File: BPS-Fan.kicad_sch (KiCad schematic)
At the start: 29 parts, among them J1 LDRBRDConn, J10 FAN9, J11 FAN10, J12 FAN11, J13 FAN12, J2 FAN1, J3 FAN2, J4 FAN3, J5 FAN4, J6 FAN5, J7 FAN6, J8 FAN7, J9 FAN8, Q1 BUK9M23-80E, Q10 BUK9M23-80E, Q4 BUK9M23-80E, Q7 BUK9M23-80E

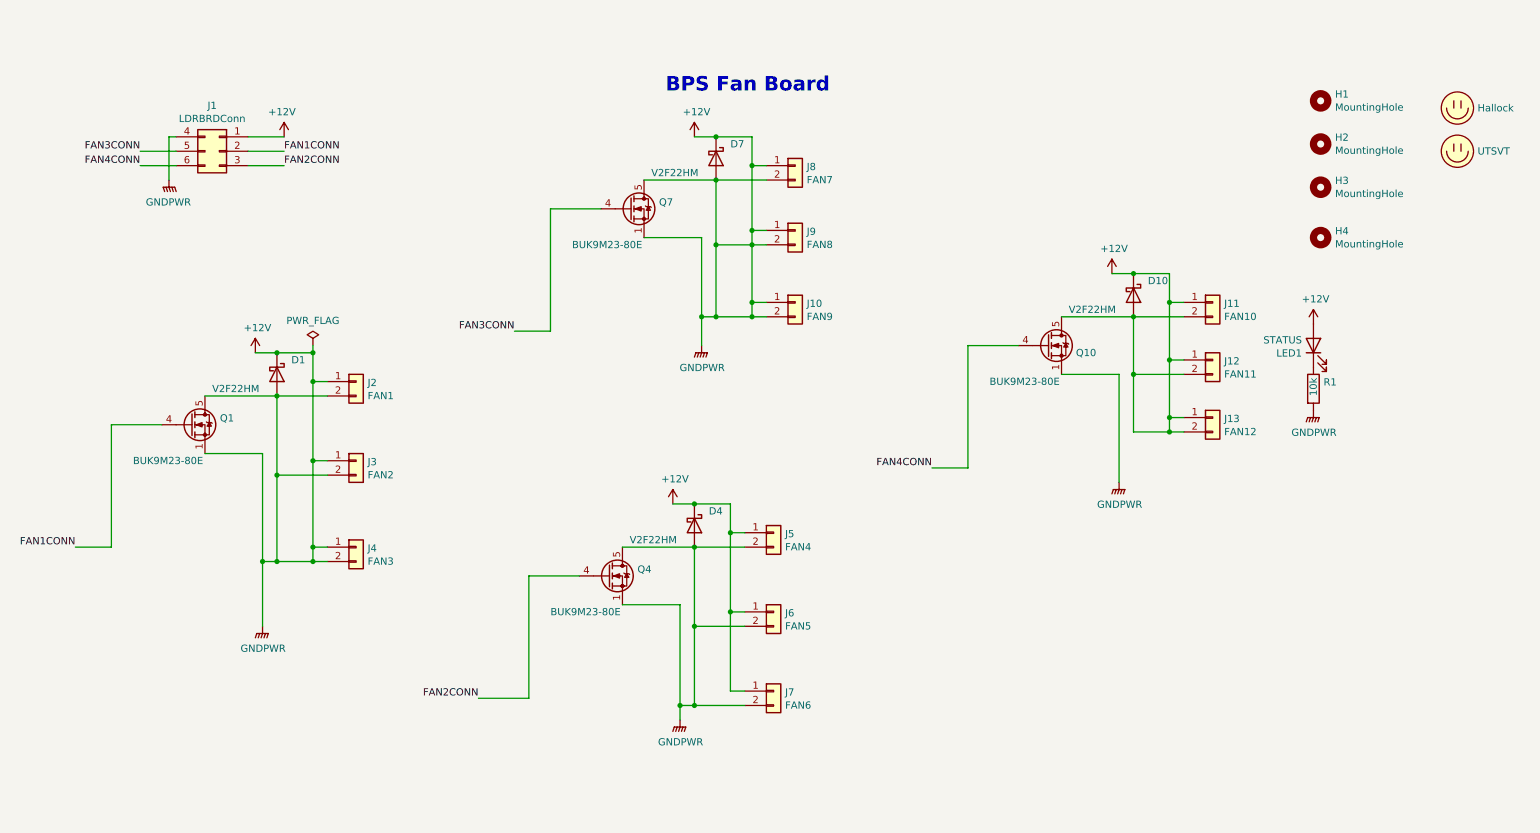
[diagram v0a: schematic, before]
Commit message: cleaned up schematic and fixed shorts
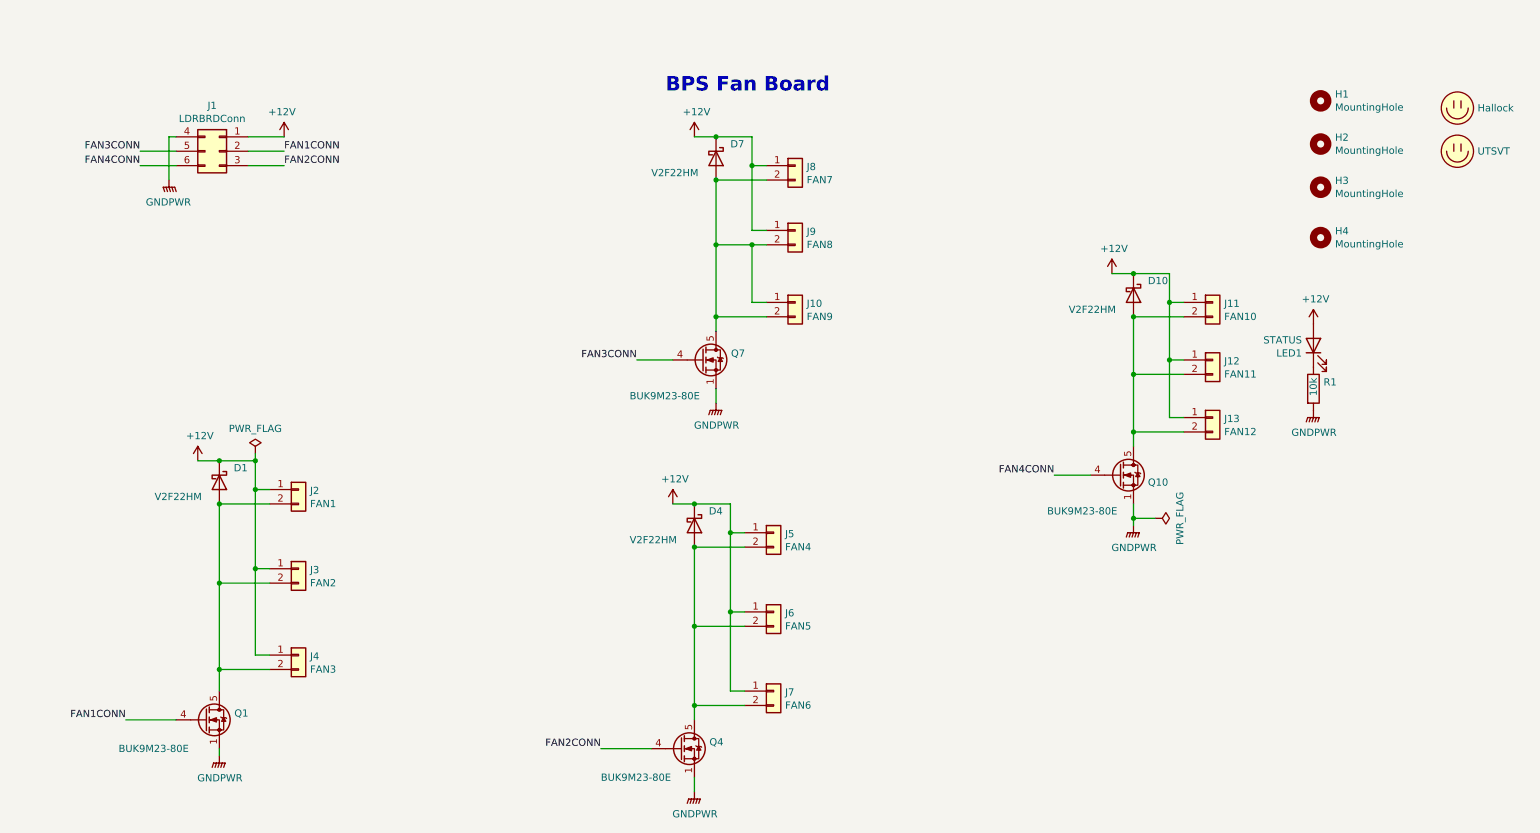
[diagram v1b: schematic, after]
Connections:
- net +12V: no longer D1.2 (A), D10.2 (A), D4.2 (A), D7.2 (A), J1.4 (Pin_4), J10.1 (Pin_1), J10.2 (Pin_2), J11.2 (Pin_2), J12.2 (Pin_2), J13.2 (Pin_2), J2.2 (Pin_2), J3.2 (Pin_2), J4.2 (Pin_2), J5.2 (Pin_2), J6.2 (Pin_2), J7.2 (Pin_2), J8.2 (Pin_2), J9.2 (Pin_2), Q1.1 (S), Q1.2 (S), Q1.3 (S), Q1.5 (D), Q10.1 (S), Q10.2 (S), Q10.3 (S), Q10.5 (D), Q4.1 (S), Q4.2 (S), Q4.3 (S), Q4.5 (D), Q7.1 (S), Q7.2 (S), Q7.3 (S), Q7.5 (D), R1.2
- new net: D10.2 (A), J11.2 (Pin_2), J12.2 (Pin_2), J13.2 (Pin_2), Q10.5 (D)
- new net: D1.2 (A), J2.2 (Pin_2), J3.2 (Pin_2), J4.2 (Pin_2), Q1.5 (D)
- new net: D4.2 (A), J5.2 (Pin_2), J6.2 (Pin_2), J7.2 (Pin_2), Q4.5 (D)
- new net: D7.2 (A), J10.1 (Pin_1), J10.2 (Pin_2), J8.2 (Pin_2), J9.2 (Pin_2), Q7.5 (D)
- new net GNDPWR: J1.4 (Pin_4), Q1.1 (S), Q1.2 (S), Q1.3 (S), Q10.1 (S), Q10.2 (S), Q10.3 (S), Q4.1 (S), Q4.2 (S), Q4.3 (S), Q7.1 (S), Q7.2 (S), Q7.3 (S), R1.2
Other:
- moved on the sheet: D1, J2, J3, J4, Q1, Q10, Q4, Q7

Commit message: fixed the last short lol
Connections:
- net +12V: now also J10.1 (Pin_1)
- net at D7.2 (A), J10.2 (Pin_2), J8.2 (Pin_2)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: no longer J10.1 (Pin_1)

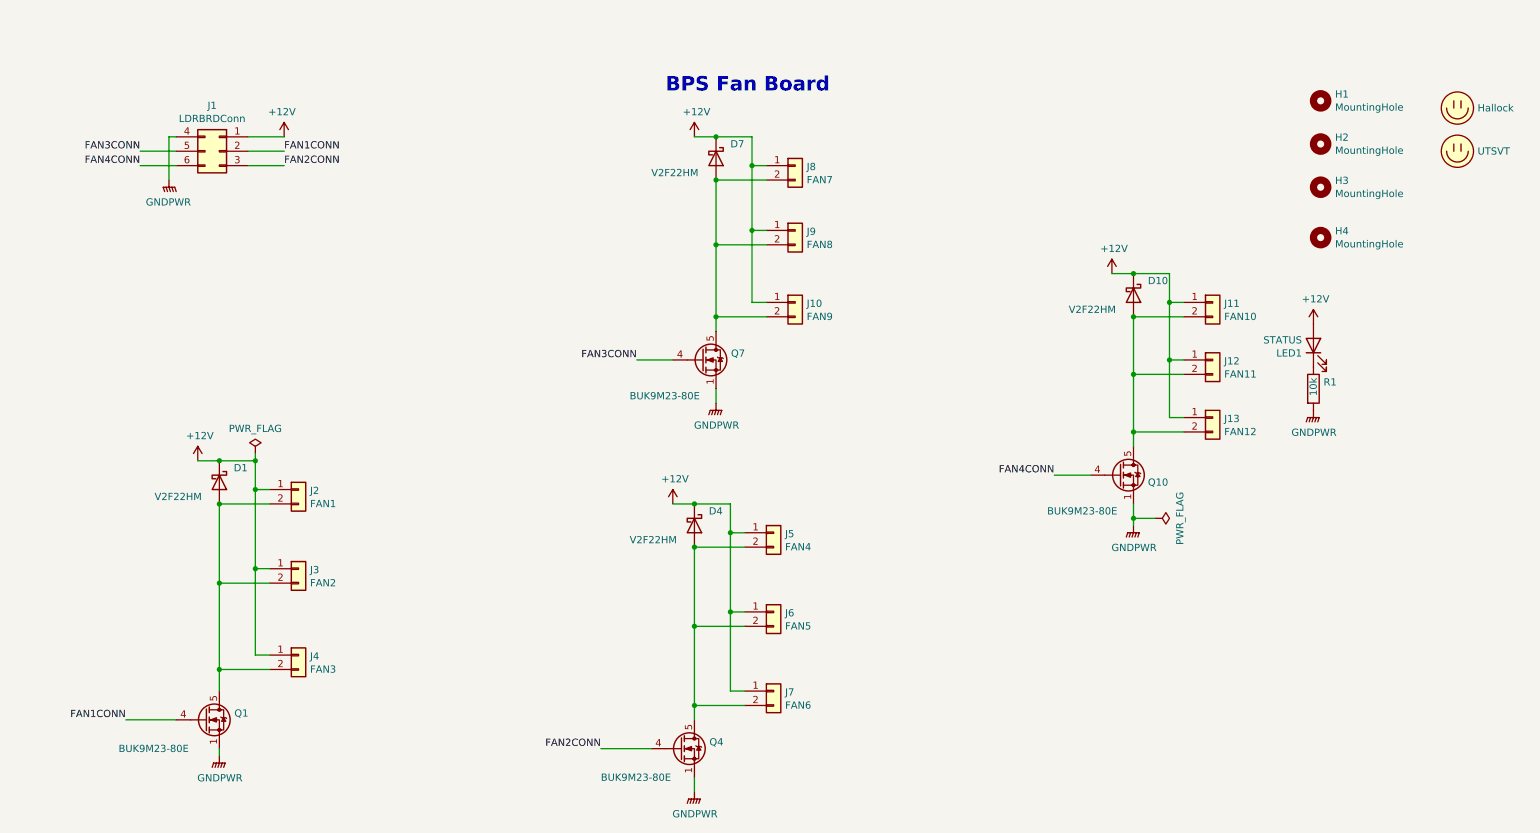
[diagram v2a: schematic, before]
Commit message: Added support for Orion
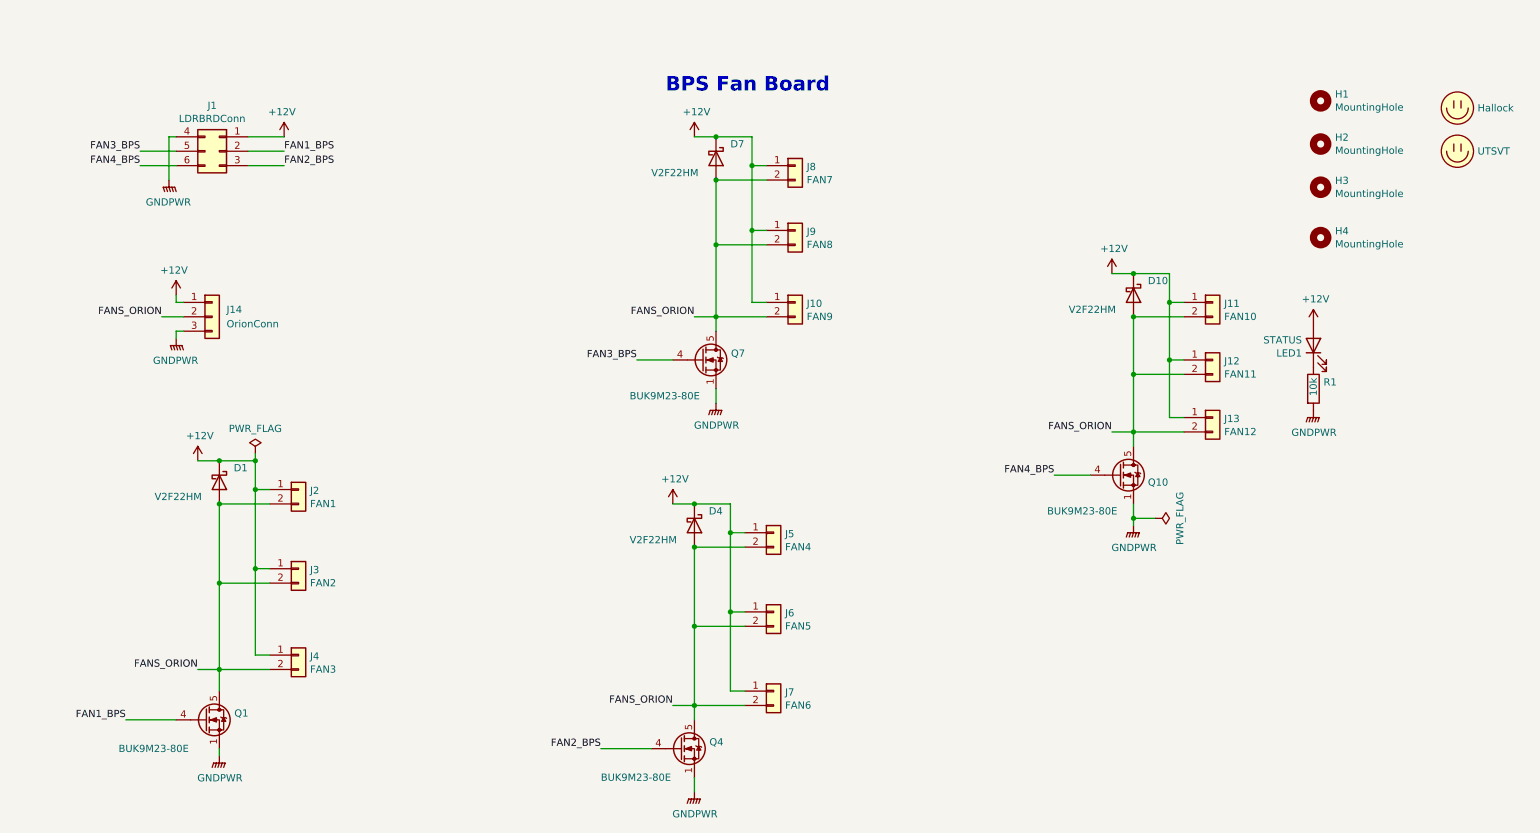
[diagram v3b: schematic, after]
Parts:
- added J14: OrionConn, symbol Connector_Generic:Conn_01x03
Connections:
- net +12V: now also J14.1 (Pin_1)
- net GNDPWR: now also J14.3 (Pin_3)
- net FANS_ORION: now reaches D10.2 (A), J11.2 (Pin_2), J12.2 (Pin_2), J13.2 (Pin_2), Q10.5 (D)
- net FANS_ORION: now also D1.2 (A), D4.2 (A), D7.2 (A), J10.2 (Pin_2), J2.2 (Pin_2), J3.2 (Pin_2), J4.2 (Pin_2), J5.2 (Pin_2), J6.2 (Pin_2), J7.2 (Pin_2), J8.2 (Pin_2), J9.2 (Pin_2), Q1.5 (D), Q4.5 (D), Q7.5 (D), J14.2 (Pin_2)
- net FAN1CONN renamed FAN1_BPS
- net FAN2CONN renamed FAN2_BPS
- net FAN3CONN renamed FAN3_BPS
- net FAN4CONN renamed FAN4_BPS
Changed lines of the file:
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@@
+    (stroke (width 0) (type default) (color 0 0 0 0))
+  )
+  (wire (pts (xy 208.28 115.57) (xy 212.09 115.57))
     (stroke (width 0) (type default) (color 0 0 0 0))
   )
@@
     (stroke (width 0) (type default) (color 0 0 0 0))
   )
+  (wire (pts (xy 134.62 95.25) (xy 138.43 95.25))
+    (stroke (width 0) (type default) (color 0 0 0 0))
+  )
   (wire (pts (xy 212.09 115.57) (xy 212.09 118.11))
     (stroke (width 0) (type default) (color 0 0 0 0))
@@
     (stroke (width 0) (type default) (color 0 0 0 0))
   )
+  (wire (pts (xy 44.45 97.79) (xy 43.18 97.79))
+    (stroke (width 0) (type default) (color 0 0 0 0))
+  )
   (wire (pts (xy 134.62 135.89) (xy 134.62 149.86))
     (stroke (width 0) (type default) (color 0 0 0 0))
@@
     (stroke (width 0) (type default) (color 0 0 0 0))
   )
+  (wire (pts (xy 43.18 92.71) (xy 44.45 92.71))
+    (stroke (width 0) (type default) (color 0 0 0 0))
+  )
   (wire (pts (xy 43.18 63.5) (xy 41.91 63.5))
     (stroke (width 0) (type default) (color 0 0 0 0))
@@
     (stroke (width 0) (type default) (color 0 0 0 0))
   )
+  (wire (pts (xy 43.18 97.79) (xy 43.18 99.06))
+    (stroke (width 0) (type default) (color 0 0 0 0))
+  )
   (wire (pts (xy 50.8 128.27) (xy 50.8 142.24))
     (stroke (width 0) (type default) (color 0 0 0 0))
@@
     (stroke (width 0) (type default) (color 0 0 0 0))
   )
+  (wire (pts (xy 138.43 82.55) (xy 147.32 82.55))
+    (stroke (width 0) (type default) (color 0 0 0 0))
+  )
+  (wire (pts (xy 134.62 176.53) (xy 134.62 179.07))
+    (stroke (width 0) (type default) (color 0 0 0 0))
+  )
+  (wire (pts (xy 43.18 91.44) (xy 43.18 92.71))
+    (stroke (width 0) (type default) (color 0 0 0 0))
+  )
+  (wire (pts (xy 140.97 128.27) (xy 134.62 128.27))
+    (stroke (width 0) (type default) (color 0 0 0 0))
+  )
+  (wire (pts (xy 62.23 63.5) (xy 55.88 63.5))
+    (stroke (width 0) (type default) (color 0 0 0 0))
+  )
+  (wire (pts (xy 140.97 133.35) (xy 140.97 147.32))
+    (stroke (width 0) (type default) (color 0 0 0 0))
+  )
+  (wire (pts (xy 130.81 163.83) (xy 134.62 163.83))
+    (stroke (width 0) (type default) (color 0 0 0 0))
+  )
+  (wire (pts (xy 59.69 154.94) (xy 57.15 154.94))
+    (stroke (width 0) (type default) (color 0 0 0 0))
+  )
+  (wire (pts (xy 218.44 87.63) (xy 212.09 87.63))
+    (stroke (width 0) (type default) (color 0 0 0 0))
+  )
   (wire (pts (xy 138.43 95.25) (xy 138.43 97.79))
     (stroke (width 0) (type default) (color 0 0 0 0))
   )
-  (wire (pts (xy 138.43 82.55) (xy 147.32 82.55))
-    (stroke (width 0) (type default) (color 0 0 0 0))
-  )
-  (wire (pts (xy 134.62 176.53) (xy 134.62 179.07))
-    (stroke (width 0) (type default) (color 0 0 0 0))
-  )
-  (wire (pts (xy 140.97 128.27) (xy 134.62 128.27))
-    (stroke (width 0) (type default) (color 0 0 0 0))
-  )
-  (wire (pts (xy 62.23 63.5) (xy 55.88 63.5))
-    (stroke (width 0) (type default) (color 0 0 0 0))
-  )
-  (wire (pts (xy 140.97 133.35) (xy 140.97 147.32))
-    (stroke (width 0) (type default) (color 0 0 0 0))
-  )
-  (wire (pts (xy 59.69 154.94) (xy 57.15 154.94))
-    (stroke (width 0) (type default) (color 0 0 0 0))
-  )
-  (wire (pts (xy 218.44 87.63) (xy 212.09 87.63))
-    (stroke (width 0) (type default) (color 0 0 0 0))
-  )
   (wire (pts (xy 140.97 147.32) (xy 140.97 161.29))
     (stroke (width 0) (type default) (color 0 0 0 0))
@@
     (stroke (width 0) (type default) (color 0 0 0 0))
   )
+  (wire (pts (xy 46.99 157.48) (xy 50.8 157.48))
+    (stroke (width 0) (type default) (color 0 0 0 0))
+  )
   (wire (pts (xy 57.15 119.38) (xy 57.15 120.65))
     (stroke (width 0) (type default) (color 0 0 0 0))
@@
   )
   (wire (pts (xy 208.28 87.63) (xy 212.09 87.63))
+    (stroke (width 0) (type default) (color 0 0 0 0))
+  )
+  (wire (pts (xy 40.64 95.25) (xy 44.45 95.25))
     (stroke (width 0) (type default) (color 0 0 0 0))
   )
@@
     (effects (font (size 2.54 2.54) (thickness 0.508) bold) (justify left bottom))
   )
-  (label "FAN1CONN" (at 62.23 66.04 0)
+  (label "FANS_ORION" (at 134.62 95.25 180)
+    (effects (font (size 1.27 1.27)) (justify right bottom))
+  )
+  (label "FANS_ORION" (at 40.64 95.25 180)
+    (effects (font (size 1.27 1.27)) (justify right bottom))
+  )
+  (label "FAN1_BPS" (at 62.23 66.04 0)
     (effects (font (size 1.27 1.27)) (justify left bottom))
   )
-  (label "FAN4CONN" (at 198.12 123.19 180)
+  (label "FANS_ORION" (at 130.81 163.83 180)
     (effects (font (size 1.27 1.27)) (justify right bottom))
   )
-  (label "FAN3CONN" (at 36.83 66.04 180)
+  (label "FANS_ORION" (at 208.28 115.57 180)
     (effects (font (size 1.27 1.27)) (justify right bottom))
   )
-  (label "FAN2CONN" (at 118.11 171.45 180)
+  (label "FAN4_BPS" (at 198.12 123.19 180)
     (effects (font (size 1.27 1.27)) (justify right bottom))
   )
-  (label "FAN2CONN" (at 62.23 68.58 0)
+  (label "FAN3_BPS" (at 36.83 66.04 180)
+    (effects (font (size 1.27 1.27)) (justify right bottom))
+  )
+  (label "FAN2_BPS" (at 118.11 171.45 180)
+    (effects (font (size 1.27 1.27)) (justify right bottom))
+  )
+  (label "FANS_ORION" (at 46.99 157.48 180)
+    (effects (font (size 1.27 1.27)) (justify right bottom))
+  )
+  (label "FAN2_BPS" (at 62.23 68.58 0)
     (effects (font (size 1.27 1.27)) (justify left bottom))
   )
-  (label "FAN3CONN" (at 124.46 102.87 180)
+  (label "FAN3_BPS" (at 124.46 102.87 180)
     (effects (font (size 1.27 1.27)) (justify right bottom))
   )
-  (label "FAN4CONN" (at 36.83 68.58 180)
+  (label "FAN4_BPS" (at 36.83 68.58 180)
     (effects (font (size 1.27 1.27)) (justify right bottom))
   )
-  (label "FAN1CONN" (at 34.29 166.37 180)
+  (label "FAN1_BPS" (at 34.29 166.37 180)
     (effects (font (size 1.27 1.27)) (justify right bottom))
   )
@@
     (pin "1")
   )
+  (symbol (lib_id "power:GNDPWR") (at 43.18 99.06 0) (mirror y) (unit 1)
+    (in_bom yes) (on_board yes)
+    (property "Reference" "#PWR07" (id 0) (at 43.18 104.14 0)
+      (effects (font (size 1.27 1.27)) hide)
+    )
+    (property "Value" "GNDPWR" (id 1) (at 43.0784 102.9716 0))
+    (property "Footprint" "" (id 2) (at 43.18 100.33 0)
+      (effects (font (size 1.27 1.27)) hide)
+    )
+    (property "Datasheet" "" (id 3) (at 43.18 100.33 0)
+      (effects (font (size 1.27 1.27)) hide)
+    )
+    (pin "1")
+  )
   (symbol (lib_id "Transistor_FET:BUK9M23-80EX") (at 209.55 123.19 0) (unit 1)
     (in_bom yes) (on_board yes)
@@
     )
     (pin "1")
+  )
+  (symbol (lib_id "Connector_Generic:Conn_01x03") (at 49.53 95.25 0) (unit 1)
+    (in_bom yes) (on_board yes) (fields_autoplaced)
+    (property "Reference" "J14" (id 0) (at 52.07 93.9799 0)
+      (effects (font (size 1.27 1.27)) (justify left))
+    )
+    (property "Value" "OrionConn" (id 1) (at 52.07 96.5199 0)
+      (effects (font (size 1.27 1.27)) (justify left))
+    )
+    (property "Footprint" "" (id 2) (at 49.53 95.25 0)
+      (effects (font (size 1.27 1.27)) hide)
+    )
+    (property "Datasheet" "~" (id 3) (at 49.53 95.25 0)
+      (effects (font (size 1.27 1.27)) hide)
+    )
+    (pin "1")
+    (pin "2")
+    (pin "3")
   )
   (symbol (lib_id "Connector_Generic:Conn_01x02") (at 152.4 92.71 0) (unit 1)
@@
     (pin "1")
   )
+  (symbol (lib_id "power:+12V") (at 43.18 91.44 0) (mirror y) (unit 1)
+    (in_bom yes) (on_board yes)
+    (property "Reference" "#PWR04" (id 0) (at 43.18 95.25 0)
+      (effects (font (size 1.27 1.27)) hide)
+    )
+    (property "Value" "+12V" (id 1) (at 42.799 87.0458 0))
+    (property "Footprint" "" (id 2) (at 43.18 91.44 0)
+      (effects (font (size 1.27 1.27)) hide)
+    )
+    (property "Datasheet" "" (id 3) (at 43.18 91.44 0)
+      (effects (font (size 1.27 1.27)) hide)
+    )
+    (pin "1")
+  )
   (symbol (lib_id "Connector_Generic:Conn_01x02") (at 226.06 113.03 0) (unit 1)
     (in_bom yes) (on_board yes)
@@
       (reference "#PWR03") (unit 1) (value "+12V") (footprint "")
     )
+    (path "/e6897cf5-5c23-442e-8a6c-8b30fd6ca137"
+      (reference "#PWR04") (unit 1) (value "+12V") (footprint "")
+    )
     (path "/00000000-0000-0000-0000-00005f1f79f1"
       (reference "#PWR05") (unit 1) (value "+12V") (footprint "")
@@
       (reference "#PWR06") (unit 1) (value "GNDPWR") (footprint "")
     )
+    (path "/2ca0c881-82f9-4ce5-8028-6b1d6bbd2303"
+      (reference "#PWR07") (unit 1) (value "GNDPWR") (footprint "")
+    )
     (path "/11dc750e-0b32-4352-8ef3-1b46bf0720f3"
       (reference "#PWR0101") (unit 1) (value "+12V") (footprint "")
@@
       (reference "J13") (unit 1) (value "FAN12") (footprint "UTSVT_Connectors:Molex_MicroFit3.0_1x2xP3.00mm_PolarizingPeg_Vertical")
     )
+    (path "/ccd06b32-5a44-41fb-a13d-537d656458f3"
+      (reference "J14") (unit 1) (value "OrionConn") (footprint "")
+    )
     (path "/00000000-0000-0000-0000-00005f1f72f0"

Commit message: Better supports for Orion
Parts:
- removed J14: OrionConn, symbol Connector_Generic:Conn_01x03
- added R? (x4): 100k, Resistor_SMD:R_0805_2012Metric, symbol Device:R
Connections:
- net +12V: now also R?.1, R?.1, R?.1, R?.1
- net FAN1_BPS: now also R?.2
- net FAN2_BPS: now also R?.2
- net FAN3_BPS: now also R?.2
- net FAN4_BPS: now also R?.2
- removed net FANS_ORION: D1.2 (A), D10.2 (A), D4.2 (A), D7.2 (A), J10.2 (Pin_2), J11.2 (Pin_2), J12.2 (Pin_2), J13.2 (Pin_2), J2.2 (Pin_2), J3.2 (Pin_2), J4.2 (Pin_2), J5.2 (Pin_2), J6.2 (Pin_2), J7.2 (Pin_2), J8.2 (Pin_2), J9.2 (Pin_2), Q1.5 (D), Q10.5 (D), Q4.5 (D), Q7.5 (D)
- new net: D10.2 (A), J11.2 (Pin_2), J12.2 (Pin_2), Q10.5 (D)
- new net: D1.2 (A), J2.2 (Pin_2), J3.2 (Pin_2), Q1.5 (D)
- new net: D7.2 (A), J8.2 (Pin_2), J9.2 (Pin_2), Q7.5 (D)
- new net: D4.2 (A), J5.2 (Pin_2), J6.2 (Pin_2), Q4.5 (D)
